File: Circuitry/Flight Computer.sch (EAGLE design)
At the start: 19 parts, among them IC1 BMP280, IC2 7805L, J1 1X2-3.5MM, J6 1X2-3.5MM, U1 MPU-6050-1

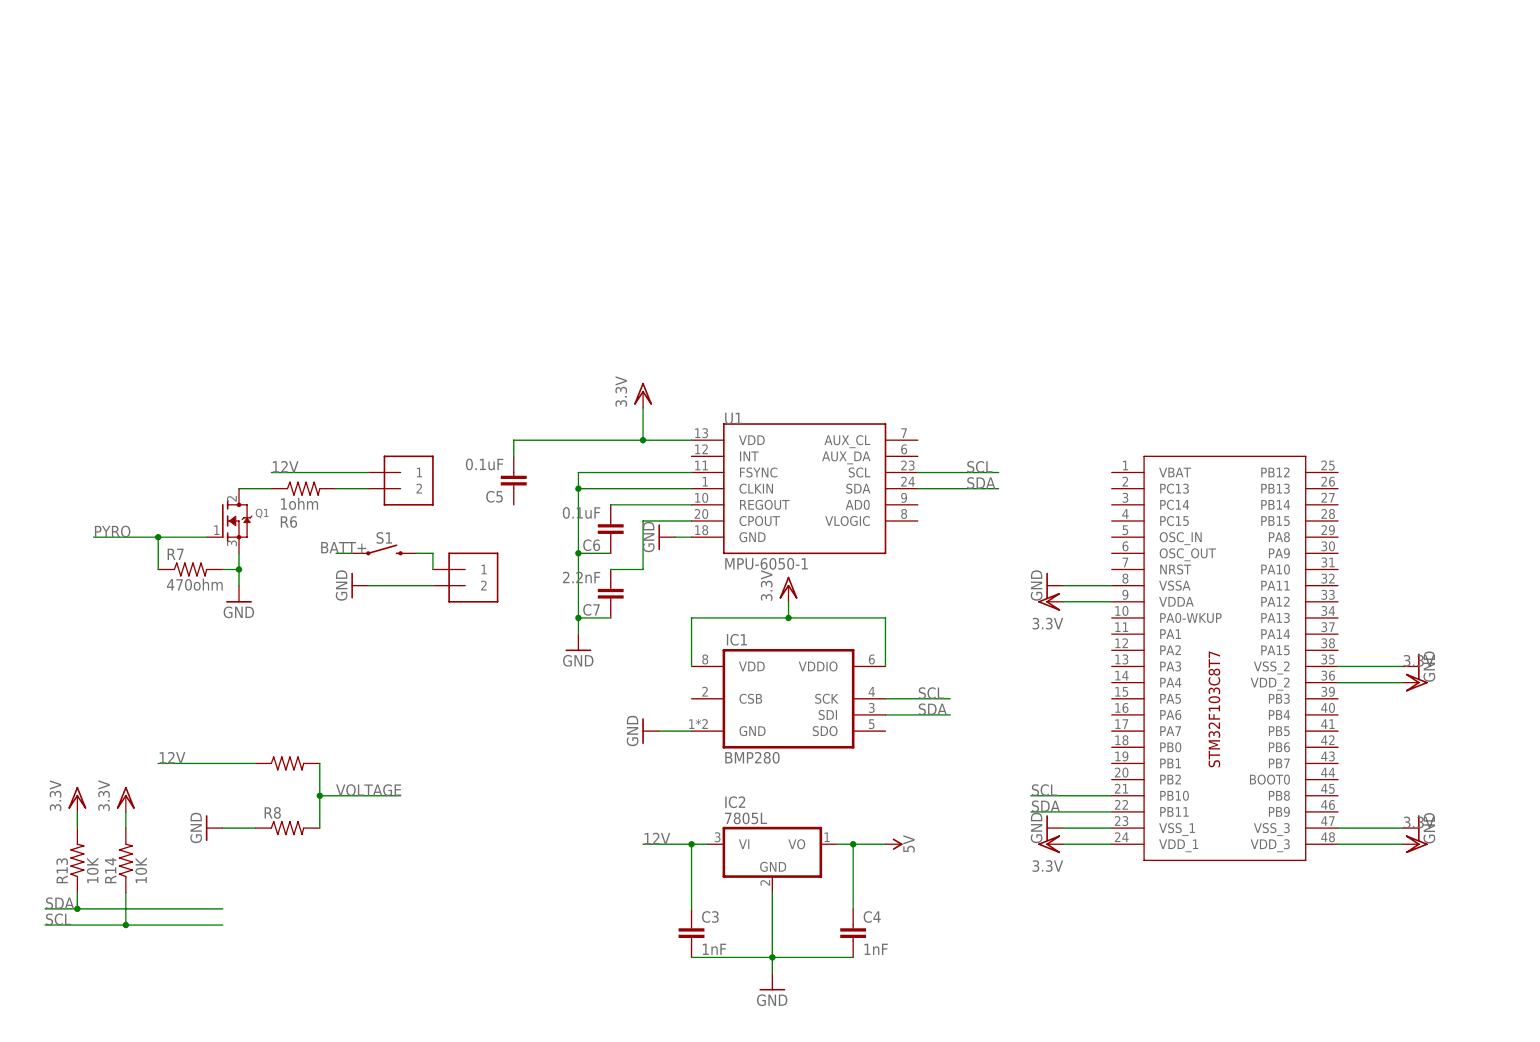
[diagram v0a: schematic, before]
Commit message: added testing computer code
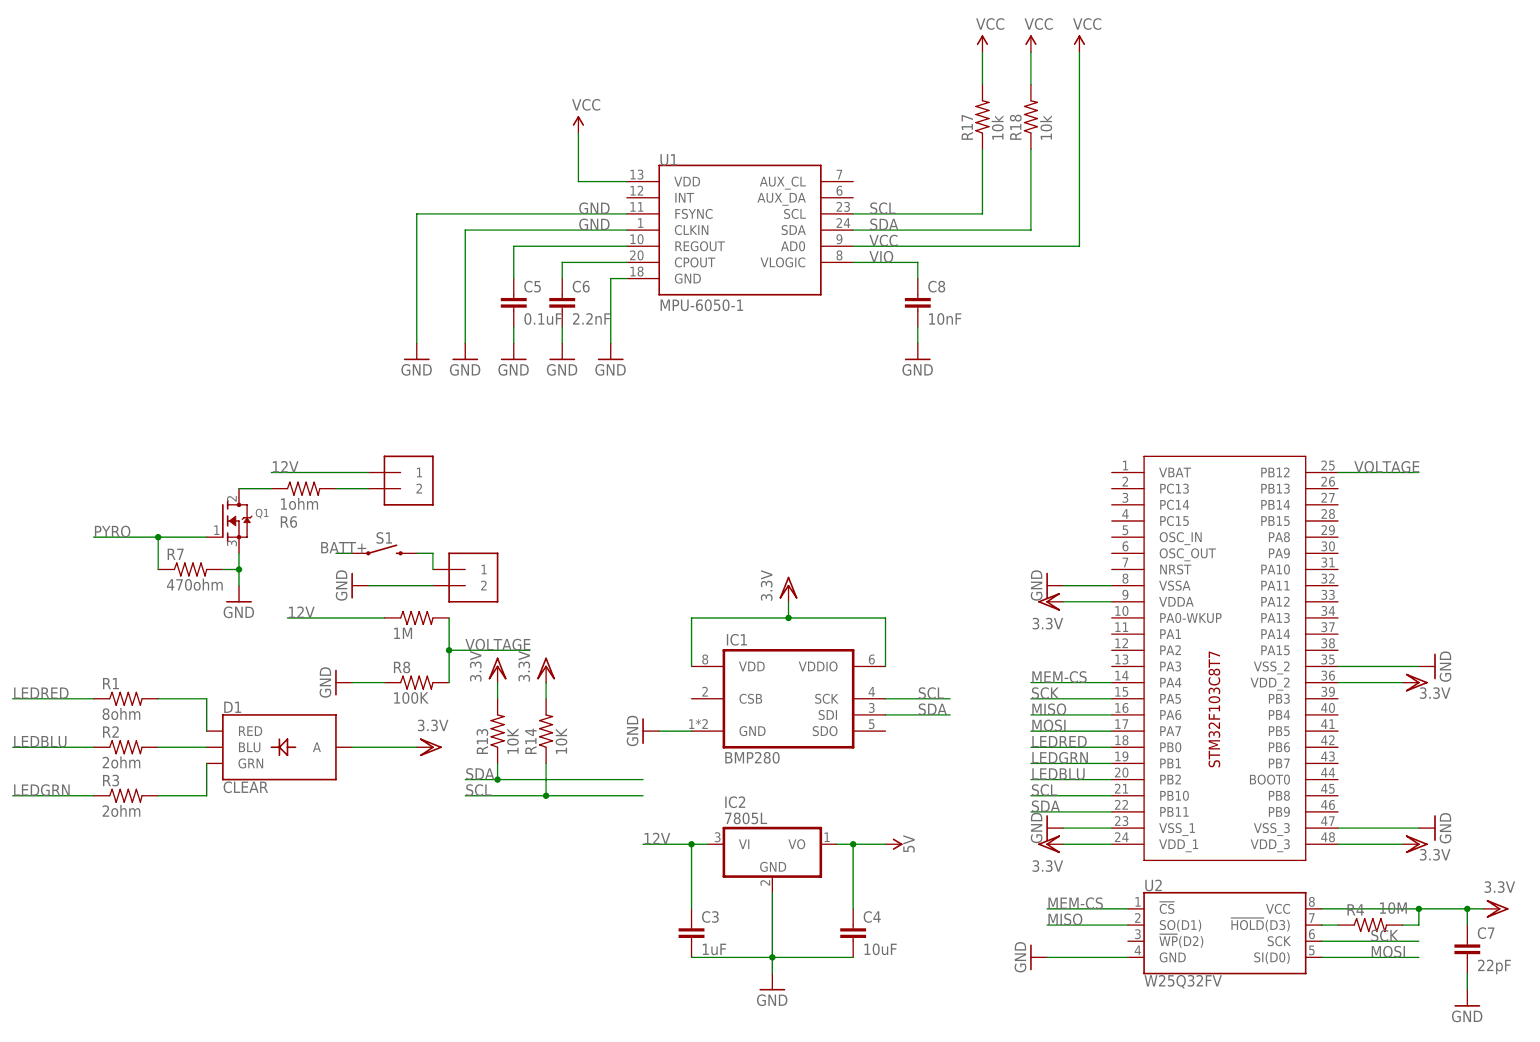
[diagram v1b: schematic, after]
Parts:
- added C8: 10nF, SparkFun:CAP0603-CAP
- added D1: CLEAR, SparkFun-LED:LED-RGB-CACLEAR
- added R1: 8ohm, adafruit:R-US_0204/2V
- added R17, R18: 10k, SparkFun:RESISTOR0603-RES
- added R2, R3: 2ohm, adafruit:R-US_0204/2V
- added R4: 10M, adafruit:R-US_0204/2V
- added U2: W25Q32FV, SparkFun-IC-Memory:W25Q32FVSS
- C3: value 1nF -> 1uF
- C4: value 1nF -> 10uF
- C5: device capacitor-wima:C2,5-3 -> SparkFun:CAP0603-CAP
- C6: value 0.1uF -> 2.2nF; device capacitor-wima:C2,5-3 -> SparkFun:CAP0603-CAP
- C7: value 2.2nF -> 22pF
- R5: value (none) -> 1M
- R8: value (none) -> 100K
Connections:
- new net LEDBLU: R2.1, U$1.PB2
- new net LEDGRN: R3.1, U$1.PB1
- new net LEDRED: R1.1, U$1.PB0
- new net MEM-CS: U$1.PA4, U2.!CS!
- new net MISO: U$1.PA6, U2.SO(D1)
- new net MOSI: U$1.PA7, U2.SI(D0)
- new net N$1: D1.RED, R1.2
- new net N$2: D1.GRN, R3.2
- new net N$3: D1.BLU, R2.2
- new net N$5: R4.1, U2.!HOLD!(D3)
- new net SCK: U$1.PA5, U2.SCK
- new net VCC: R17.2, R18.2, U1.AD0, U1.VDD
- new net VIO: C8.1, U1.VLOGIC
- net GND: now also C5.2, C6.2, C7.2, C8.2, U2.GND; no longer C6.1, C7.1
- net N$11: now also C6.1; no longer C7.2
- net N$12: now also C5.1; no longer C6.2
- net SCL: now also R17.1
- net SDA: now also R18.1
- net VDD: now also C7.1, D1.A, R4.2, U2.VCC; no longer C5.2, U1.VDD
- net VOLTAGE: now also U$1.PB12
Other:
- moved on the sheet: C5, C6, C7, R13, R14, R8, U1
